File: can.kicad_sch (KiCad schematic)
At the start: 43 parts, among them Q3 2N7002, U5 TJA1051T/3, U6 MCP2518FD, U7 TJA1051T/3, Y1 40MHz

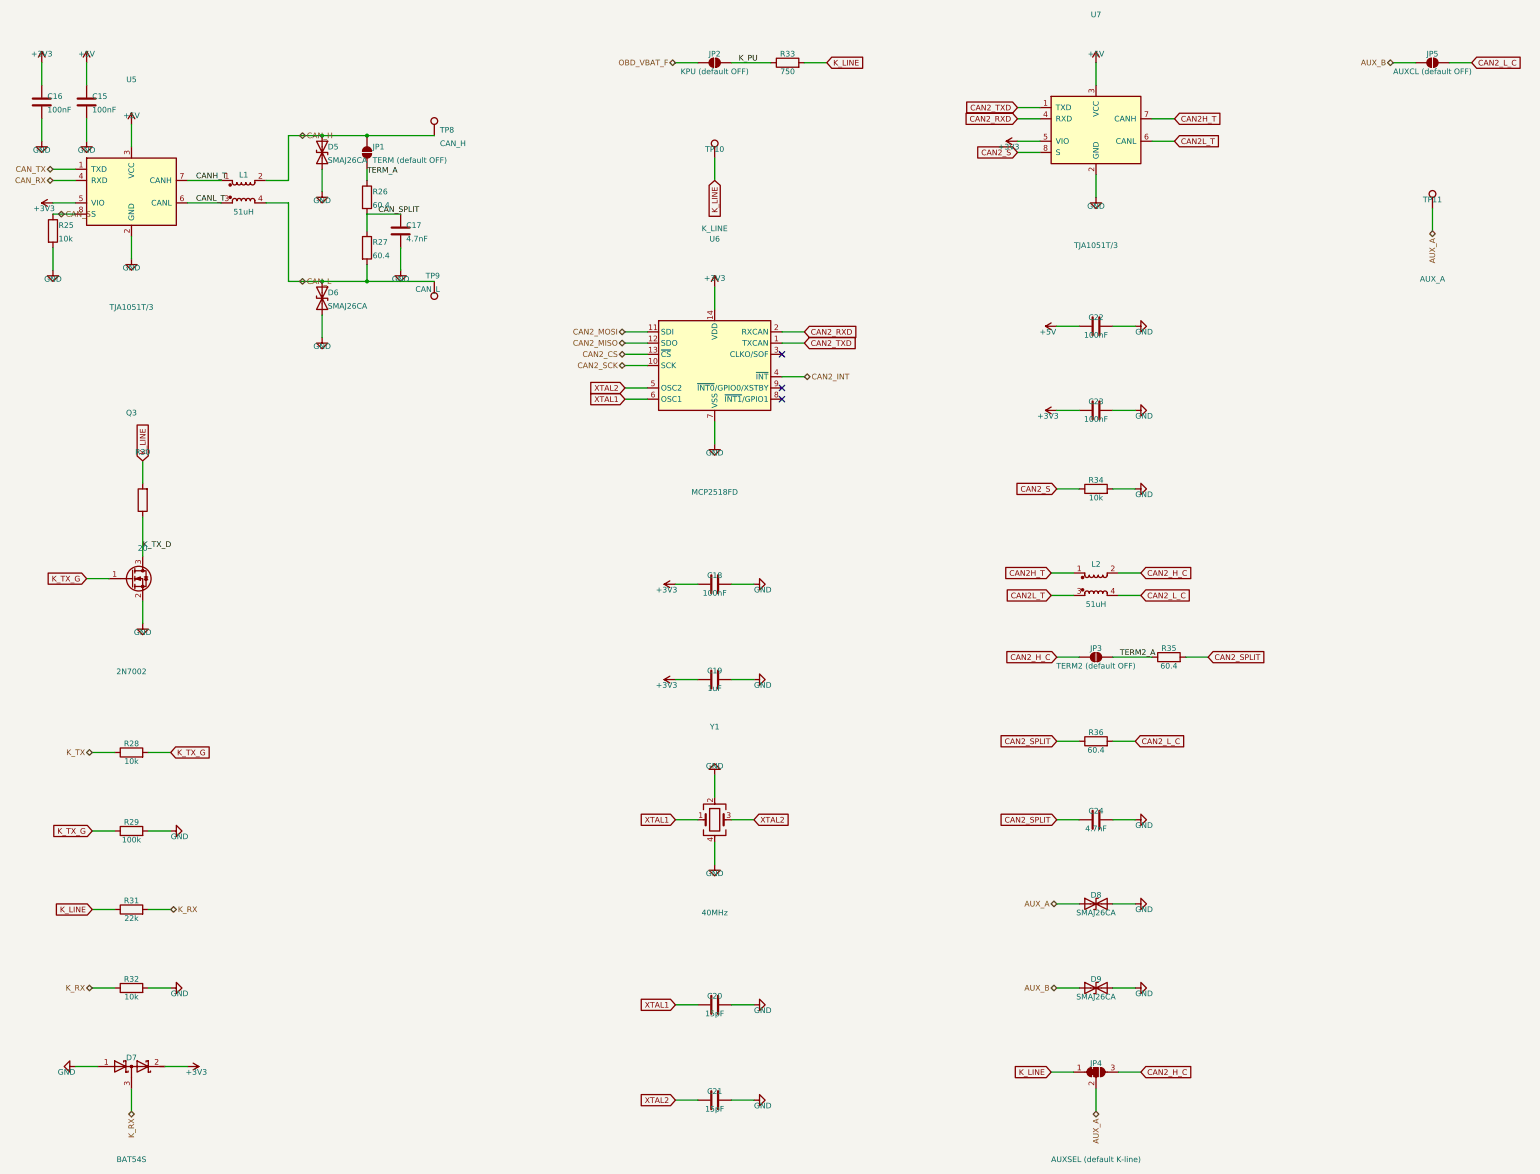
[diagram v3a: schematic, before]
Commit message: Make the schematic readable: wire the loose parts, stop text printing through symbols
Three things the drawing was doing badly, all now measured by a new
gen/audit_schematic.py rather than judged by eye.

LOOSE PARTS ARE WIRED NOW. A decoupling capacitor is a two-pin part with a
rail on each pin, and the column packer had no reason to put one next to
another -- so each came out as its own island with a net label at both ends,
twenty-odd of them down the edge of the power sheet. Electrically perfect,
visually a parts bin. build_ladders() groups the leftovers by which pair of
nets they sit across and draws each group as a proper ladder: one wire along
the top pins, one along the bottom, a junction at every rung and a power
symbol at each end. Nine groups across five sheets, including the supercap
bank and the battery monitor, and it removes two labels per part.

Grouping is on the actual pin GEOMETRY, not the symbol name, which is what
lets a balancing resistor share a ladder with the capacitor it balances while
keeping out a TVS diode whose pins are 1.3 mm closer together -- that one ERC
caught as two unconnected wire endpoints.

TEXT NO LONGER PRINTS THROUGH SYMBOLS. The offsets that place a reference and
a value work from the box around a part's PINS, and a symbol's graphic is
routinely drawn outside it. A power symbol's arrow therefore went straight
through its own name -- "+5VS" read "+2VS" at a glance, which is exactly how
somebody ends up probing the wrong rail -- and a capacitor lying on its side
has a y extent of exactly zero, so its reference and value printed across the
plates. Both now work from a floor on the body size. Rail names are also
centred on their own pin instead of drooping half a pitch onto the next one,
and the solder jumpers lost "(default OFF)" from their value into their note,
which is eighteen characters of text on a part 1.3 mm wide.

THE HAND-DRAWN BLOCKS WERE RE-SPACED to suit, because their tables were laid
out when the text sat closer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
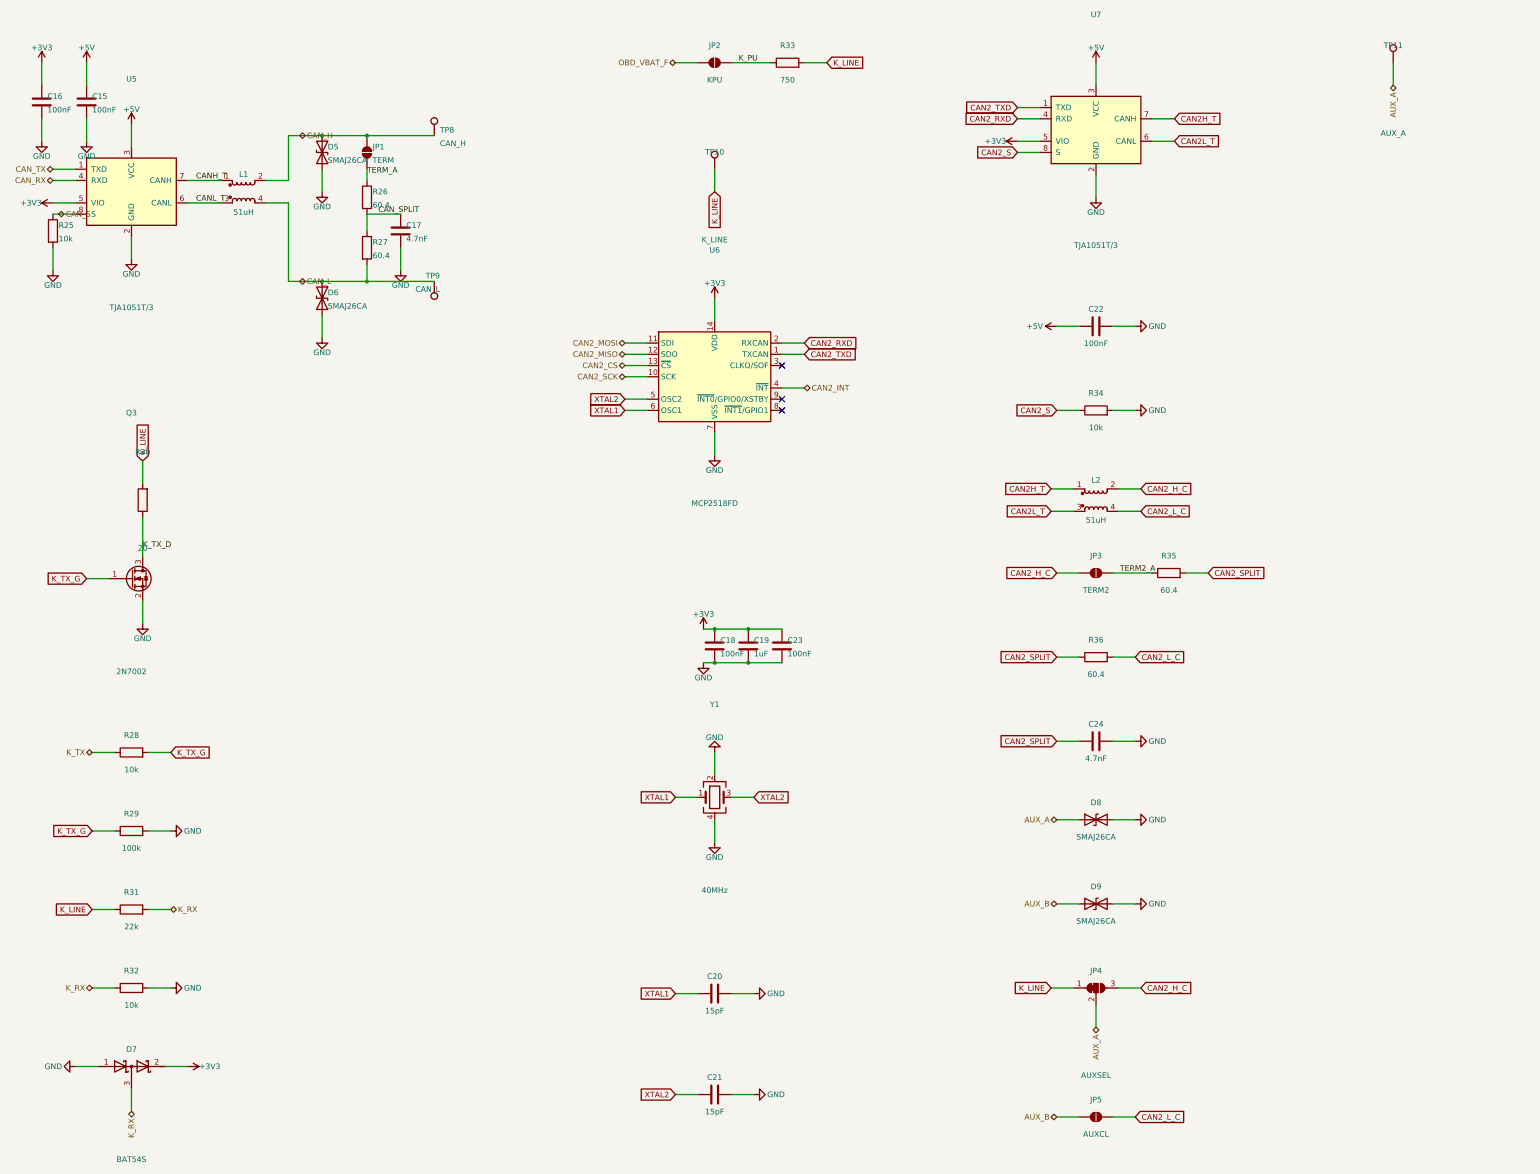
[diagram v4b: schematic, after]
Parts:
- JP1: value TERM (default OFF) -> TERM
- JP2: value KPU (default OFF) -> KPU
- JP3: value TERM2 (default OFF) -> TERM2
- JP4: value AUXSEL (default K-line) -> AUXSEL
- JP5: value AUXCL (default OFF) -> AUXCL
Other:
- moved on the sheet: C18, C19, C20, C21, C23, C24, D8, D9, JP3, JP4, JP5, L2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
